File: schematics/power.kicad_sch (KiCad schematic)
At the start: 39 parts, among them J1 9VRMS_60HZ, SW1 SW_SPDT, SW2 SW_Push, SW3 SW_Push, SW4 SW_Push, U1 74HC14, U2 LM2576T-ADJ, U3 LM337T

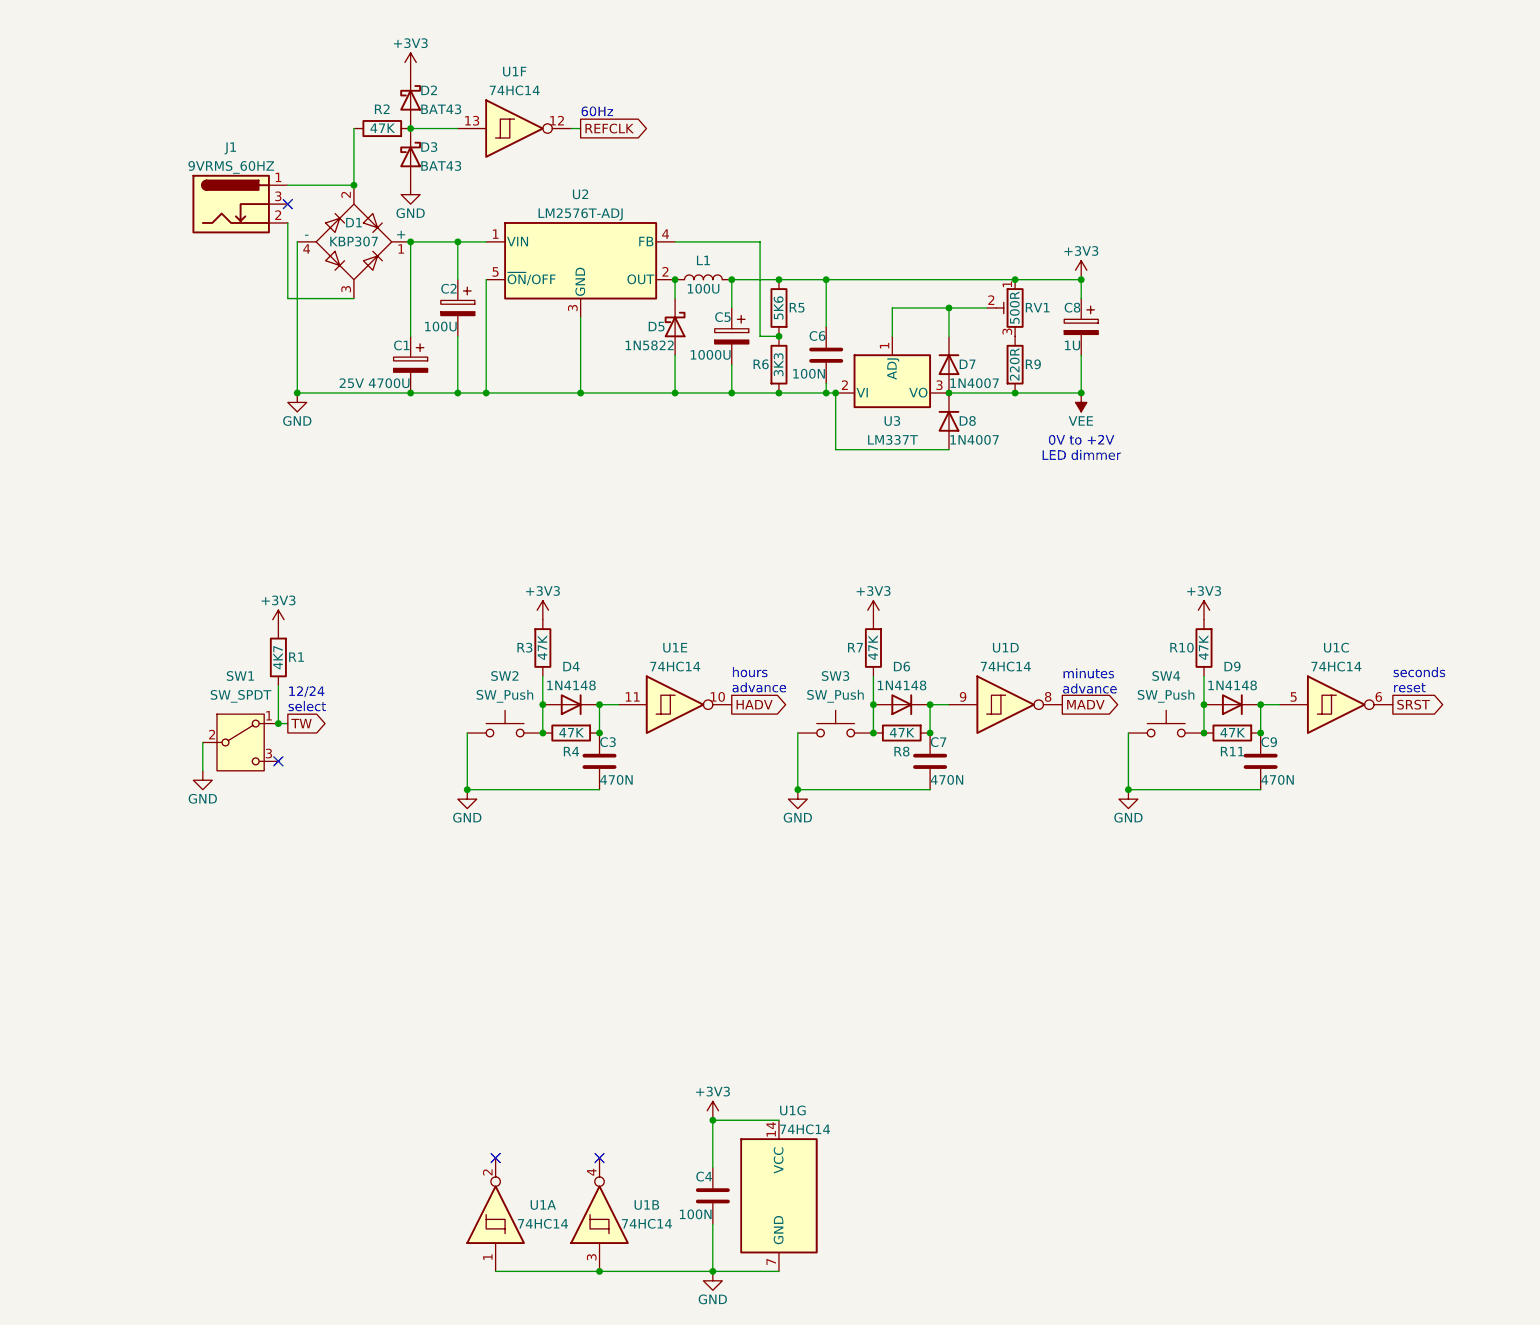
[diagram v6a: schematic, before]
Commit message: switched to PWM for LEDs
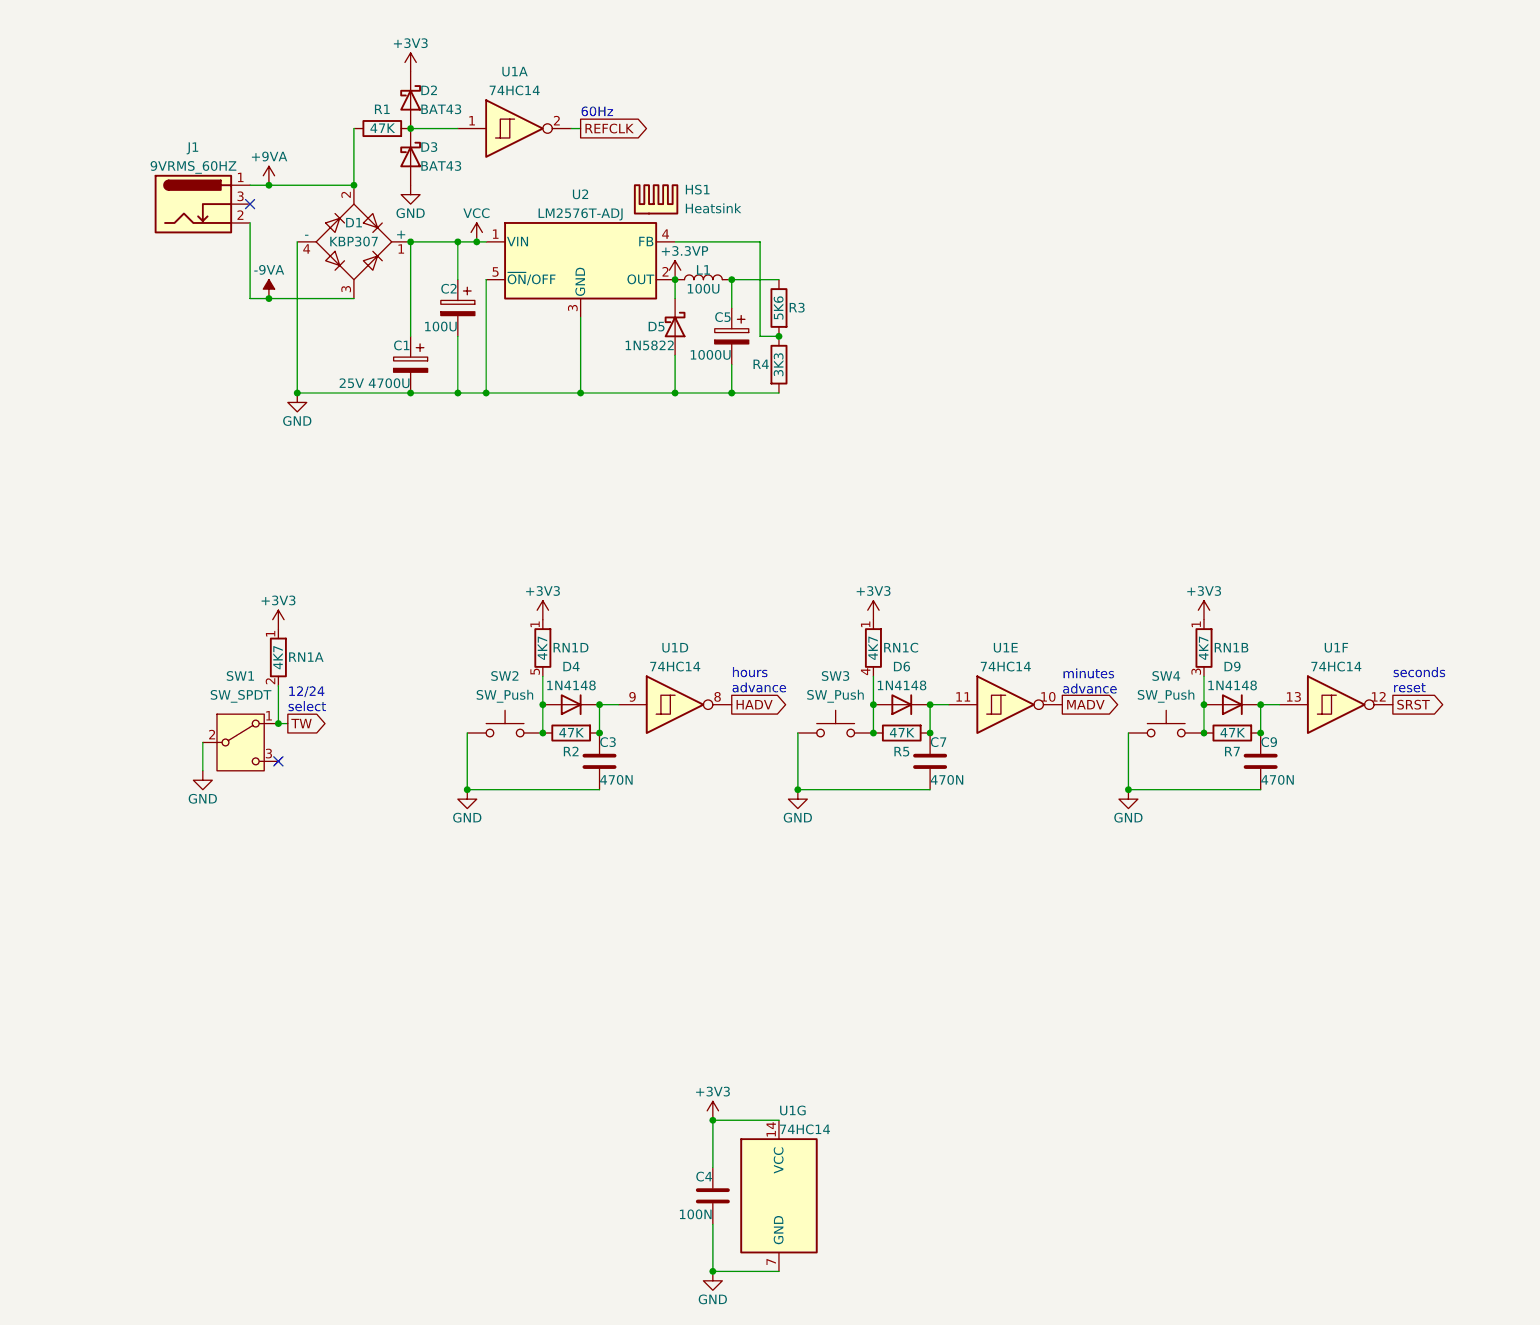
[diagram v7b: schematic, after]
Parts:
- removed C6: 100N, Capacitor_THT:C_Disc_D5.1mm_W3.2mm_P5.00mm, symbol Device:C
- removed C8: 1U, Capacitor_THT:CP_Radial_D5.0mm_P2.00mm, symbol Device:C_Polarized
- removed D7, D8: 1N4007, Diode_THT:D_DO-41_SOD81_P10.16mm_Horizontal, symbol Diode:1N4007
- removed R1: 4K7, Resistor_THT:R_Axial_DIN0207_L6.3mm_D2.5mm_P10.16mm_Horizontal, symbol Device:R
- removed R10, R3, R7: 47K, Resistor_THT:R_Axial_DIN0207_L6.3mm_D2.5mm_P10.16mm_Horizontal, symbol Device:R
- removed R9: 220R, Resistor_THT:R_Axial_DIN0207_L6.3mm_D2.5mm_P10.16mm_Horizontal, symbol Device:R
- removed RV1: 500R, Potentiometer_THT:Potentiometer_Vishay_T73YP_Vertical, symbol Device:R_Potentiometer_Trim
- removed unit 2 of U1
- removed unit 1 of U1
- removed U3: LM337T, Package_TO_SOT_THT:TO-220-3_Vertical, symbol Regulator_Linear:LM337_TO220
- added HS1: Heatsink, bvclock:Heatsink_TO-220, symbol Mechanical:Heatsink
- added RN1: 4K7, Resistor_THT:R_Array_SIP5, symbol Device:R_Network04_Split
- C1: footprint Capacitor_THT:C_Radial_D16.0mm_H25.0mm_P7.50mm -> Capacitor_THT:CP_Radial_D16.0mm_P7.50mm
- C2: footprint Capacitor_THT:C_Radial_D5.0mm_H11.0mm_P2.00mm -> Capacitor_THT:CP_Radial_D5.0mm_P2.00mm
- R1: renamed from R2; footprint Resistor_THT:R_Axial_DIN0207_L6.3mm_D2.5mm_P10.16mm_Horizontal -> Resistor_THT:R_Axial_DIN0207_L6.3mm_D2.5mm_P7.62mm_Horizontal
- R2: renamed from R4; footprint Resistor_THT:R_Axial_DIN0207_L6.3mm_D2.5mm_P10.16mm_Horizontal -> Resistor_THT:R_Axial_DIN0207_L6.3mm_D2.5mm_P7.62mm_Horizontal
- R3: renamed from R5; footprint Resistor_THT:R_Axial_DIN0207_L6.3mm_D2.5mm_P10.16mm_Horizontal -> Resistor_THT:R_Axial_DIN0207_L6.3mm_D2.5mm_P7.62mm_Horizontal
- R4: renamed from R6; footprint Resistor_THT:R_Axial_DIN0207_L6.3mm_D2.5mm_P10.16mm_Horizontal -> Resistor_THT:R_Axial_DIN0207_L6.3mm_D2.5mm_P7.62mm_Horizontal
- R5: renamed from R8; footprint Resistor_THT:R_Axial_DIN0207_L6.3mm_D2.5mm_P10.16mm_Horizontal -> Resistor_THT:R_Axial_DIN0207_L6.3mm_D2.5mm_P7.62mm_Horizontal
- R7: renamed from R11; footprint Resistor_THT:R_Axial_DIN0207_L6.3mm_D2.5mm_P10.16mm_Horizontal -> Resistor_THT:R_Axial_DIN0207_L6.3mm_D2.5mm_P7.62mm_Horizontal
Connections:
- net +3V3: now also RN1.1 (R1), RN1.1 (R1), RN1.1 (R1), RN1.1 (R1); no longer C5.1, L1.2, R3.1
- net HADV: now also U1.8; no longer U1.10
- net MADV: now also U1.10; no longer U1.8
- net REFCLK: now also U1.2; no longer U1.12
- net SRST: now also U1.12; no longer U1.6
- net TW: now also RN1.2 (R1.2)
- net at C3.1, D4.1 (K), R2.2: now also U1.9; no longer U1.11
- net at D2.2 (A), D3.1 (K), R1.2: now also U1.1; no longer U1.13
- net at D4.2 (A), R2.1, SW2.2: now also RN1.5 (R4.2)
- net VCC: now reaches C1.1, C2.1, D1.1 (+), U2.1 (VIN)
- net +3.3VP: now reaches D5.1 (K), L1.1, U2.2 (OUT)
- net at D6.2 (A), R5.1, SW3.2: now also RN1.4 (R3.2)
- net at C7.1, D6.1 (K), R5.2: now also U1.11; no longer U1.9
- net at C9.1, D9.1 (K), R7.2: now also U1.13; no longer U1.5
- net at D9.2 (A), R7.1, SW4.2: now also RN1.3 (R2.2)
- net +9VA: now reaches D1.2, J1.1, R1.1
- net -9VA: now reaches D1.3, J1.2
- new net: C5.1, L1.2, R3.1
- no-connect marks 4 -> 2
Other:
- note removed: "0V to +2V LED dimmer"
- moved on the sheet: J1

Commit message: fiddled with transistors
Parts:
- renumbered C7 to C6, C9 to C7, D9 to D7, R7 to R6
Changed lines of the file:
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@@
 		(in_pos_files yes)
 		(dnp no)
-		(property "Reference" "#PWR064"
+		(property "Reference" "#PWR03"
 			(at 82.55 71.12 0)
 			(hide yes)
@@
 			(project "bvclock"
 				(path "/c60296a7-2d90-476d-9ba8-593ef9b0941e/f5e86072-9c14-4298-882e-305fc24f4757"
-					(reference "#PWR064")
+					(reference "#PWR03")
 					(unit 1)
 				)
@@
 		(in_pos_files yes)
 		(dnp no)
-		(property "Reference" "#PWR03"
+		(property "Reference" "#PWR05"
 			(at 86.36 86.36 0)
 			(hide yes)
@@
 			(project "bvclock"
 				(path "/c60296a7-2d90-476d-9ba8-593ef9b0941e/f5e86072-9c14-4298-882e-305fc24f4757"
-					(reference "#PWR03")
+					(reference "#PWR05")
 					(unit 1)
 				)
@@
 		(in_pos_files yes)
 		(dnp no)
-		(property "Reference" "#PWR012"
+		(property "Reference" "#PWR02"
 			(at 82.55 55.245 0)
 			(hide yes)
@@
 			(project "bvclock"
 				(path "/c60296a7-2d90-476d-9ba8-593ef9b0941e/f5e86072-9c14-4298-882e-305fc24f4757"
-					(reference "#PWR012")
+					(reference "#PWR02")
 					(unit 1)
 				)
@@
 		(in_pos_files yes)
 		(dnp no)
-		(property "Reference" "#PWR011"
+		(property "Reference" "#PWR014"
 			(at 153.67 139.7 0)
 			(hide yes)
@@
 			(project "bvclock"
 				(path "/c60296a7-2d90-476d-9ba8-593ef9b0941e/f5e86072-9c14-4298-882e-305fc24f4757"
-					(reference "#PWR011")
+					(reference "#PWR014")
 					(unit 1)
 				)
@@
 		(in_pos_files yes)
 		(dnp no)
-		(property "Reference" "D9"
+		(property "Reference" "D7"
 			(at 212.09 116.84 0)
 			(show_name no)
@@
 			(project "bvclock"
 				(path "/c60296a7-2d90-476d-9ba8-593ef9b0941e/f5e86072-9c14-4298-882e-305fc24f4757"
-					(reference "D9")
+					(reference "D7")
 					(unit 1)
 				)
@@
 		(in_pos_files yes)
 		(dnp no)
-		(property "Reference" "#PWR07"
+		(property "Reference" "#PWR010"
 			(at 119.38 114.3 0)
 			(hide yes)
@@
 			(project "bvclock"
 				(path "/c60296a7-2d90-476d-9ba8-593ef9b0941e/f5e86072-9c14-4298-882e-305fc24f4757"
-					(reference "#PWR07")
+					(reference "#PWR010")
 					(unit 1)
 				)
@@
 		(in_pos_files yes)
 		(dnp no)
-		(property "Reference" "#PWR065"
+		(property "Reference" "#PWR011"
 			(at 140.97 66.04 0)
 			(hide yes)
@@
 			(project "bvclock"
 				(path "/c60296a7-2d90-476d-9ba8-593ef9b0941e/f5e86072-9c14-4298-882e-305fc24f4757"
-					(reference "#PWR065")
+					(reference "#PWR011")
 					(unit 1)
 				)
@@
 		(in_pos_files yes)
 		(dnp no)
-		(property "Reference" "#PWR05"
+		(property "Reference" "#PWR07"
 			(at 101.6 58.42 0)
 			(hide yes)
@@
 			(project "bvclock"
 				(path "/c60296a7-2d90-476d-9ba8-593ef9b0941e/f5e86072-9c14-4298-882e-305fc24f4757"
-					(reference "#PWR05")
+					(reference "#PWR07")
 					(unit 1)
 				)
@@
 		(in_pos_files yes)
 		(dnp no)
-		(property "Reference" "#PWR06"
+		(property "Reference" "#PWR08"
 			(at 109.22 139.7 0)
 			(hide yes)
@@
 			(project "bvclock"
 				(path "/c60296a7-2d90-476d-9ba8-593ef9b0941e/f5e86072-9c14-4298-882e-305fc24f4757"
-					(reference "#PWR06")
+					(reference "#PWR08")
 					(unit 1)
 				)
@@
 		(in_pos_files yes)
 		(dnp no)
-		(property "Reference" "#PWR08"
+		(property "Reference" "#PWR09"
 			(at 110.49 63.5 0)
 			(hide yes)
@@
 			(project "bvclock"
 				(path "/c60296a7-2d90-476d-9ba8-593ef9b0941e/f5e86072-9c14-4298-882e-305fc24f4757"
-					(reference "#PWR08")
+					(reference "#PWR09")
 					(unit 1)
 				)
@@
 		(in_pos_files yes)
 		(dnp no)
-		(property "Reference" "#PWR013"
+		(property "Reference" "#PWR015"
 			(at 163.83 114.3 0)
 			(hide yes)
@@
 			(project "bvclock"
 				(path "/c60296a7-2d90-476d-9ba8-593ef9b0941e/f5e86072-9c14-4298-882e-305fc24f4757"
-					(reference "#PWR013")
+					(reference "#PWR015")
 					(unit 1)
 				)
@@
 		(in_pos_files yes)
 		(dnp no)
-		(property "Reference" "R7"
+		(property "Reference" "R6"
 			(at 212.09 128.27 90)
 			(show_name no)
@@
 			(project "bvclock"
 				(path "/c60296a7-2d90-476d-9ba8-593ef9b0941e/f5e86072-9c14-4298-882e-305fc24f4757"
-					(reference "R7")
+					(reference "R6")
 					(unit 1)
 				)
@@
 		(in_pos_files yes)
 		(dnp no)
-		(property "Reference" "#PWR09"
+		(property "Reference" "#PWR012"
 			(at 142.24 181.61 0)
 			(hide yes)
@@
 			(project "bvclock"
 				(path "/c60296a7-2d90-476d-9ba8-593ef9b0941e/f5e86072-9c14-4298-882e-305fc24f4757"
-					(reference "#PWR09")
+					(reference "#PWR012")
 					(unit 1)
 				)
@@
 		(in_pos_files yes)
 		(dnp no)
-		(property "Reference" "#PWR04"
+		(property "Reference" "#PWR06"
 			(at 101.6 40.64 0)
 			(hide yes)
@@
 			(project "bvclock"
 				(path "/c60296a7-2d90-476d-9ba8-593ef9b0941e/f5e86072-9c14-4298-882e-305fc24f4757"
-					(reference "#PWR04")
+					(reference "#PWR06")
 					(unit 1)
 				)
@@
 		(in_pos_files yes)
 		(dnp no)
-		(property "Reference" "C7"
+		(property "Reference" "C6"
 			(at 171.45 127 0)
 			(show_name no)
@@
 			(project "bvclock"
 				(path "/c60296a7-2d90-476d-9ba8-593ef9b0941e/f5e86072-9c14-4298-882e-305fc24f4757"
-					(reference "C7")
+					(reference "C6")
 					(unit 1)
 				)
@@
 		(in_pos_files yes)
 		(dnp no)
-		(property "Reference" "C9"
+		(property "Reference" "C7"
 			(at 215.9 127 0)
 			(show_name no)
@@
 			(project "bvclock"
 				(path "/c60296a7-2d90-476d-9ba8-593ef9b0941e/f5e86072-9c14-4298-882e-305fc24f4757"
-					(reference "C9")
+					(reference "C7")
 					(unit 1)
 				)
@@
 		(in_pos_files yes)
 		(dnp no)
-		(property "Reference" "#PWR010"
+		(property "Reference" "#PWR013"
 			(at 142.24 204.47 0)
 			(hide yes)
@@
 			(project "bvclock"
 				(path "/c60296a7-2d90-476d-9ba8-593ef9b0941e/f5e86072-9c14-4298-882e-305fc24f4757"
-					(reference "#PWR010")
+					(reference "#PWR013")
 					(unit 1)
 				)
@@
 		(in_pos_files yes)
 		(dnp no)
-		(property "Reference" "#PWR02"
+		(property "Reference" "#PWR04"
 			(at 83.82 115.57 0)
 			(hide yes)
@@
 			(project "bvclock"
 				(path "/c60296a7-2d90-476d-9ba8-593ef9b0941e/f5e86072-9c14-4298-882e-305fc24f4757"
-					(reference "#PWR02")
+					(reference "#PWR04")
 					(unit 1)
 				)
